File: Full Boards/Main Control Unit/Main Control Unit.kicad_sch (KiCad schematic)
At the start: 405 parts, among them J1 Optional Bond, J2 Future Use, J3 Conn_01x02_Pin, Q1 DMN6075S, Q10 DMN6075S, Q11 BSS314PE, Q12 DMN6075S, Q13 BSS314PE, Q14 DMN6075S, Q15 DMN6075S, Q2 BSS314PE, Q3 DMN6075S, Q4 BSS314PE, Q5 DMN6075S, Q6 DMN6075S, Q7 DMN6075S, Q8 DMN6075S, Q9 BSS314PE, SW1 Boot, SW2 Reset, T1 760390014, T2 760390014

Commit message: Finishing touches on the PCB layout.
Signed-off-by: digimer <digital.mermaid@gmail.com>
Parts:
- TP13: value Throttle Pots -> Throttle Pot
- TP14: value Regen Pots -> Regen Pot
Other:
- note added: "D-Sub shells are DC-floating and AC-referenced to ship ground through C83-C86"
- note removed: "Pour ground plane for GND_SH15F"
- note removed: "Pour ground plane for GND_SH15M"
- note removed: "Pour ground plane for GND_SH25F"
- note removed: "Pour ground plane for GND_SH9M"
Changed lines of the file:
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@@
 		(title "Main Control Unit")
 		(date "2026-07-29")
-		(rev "1.6.6")
+		(rev "1.6.7")
 		(company "The Digital Mermaid")
 	)
@@
 		)
 	)
-	(text "Pour ground plane for GND_SH25F"
+	(text "D-Sub shells are DC-floating and AC-referenced to ship ground through C83-C86"
 		(exclude_from_sim no)
-		(at 32.258 523.748 0)
+		(at 56.134 526.796 0)
 		(effects
 			(font
@@
 		)
 	)
-	(text "Pour ground plane for GND_SH15F"
-		(exclude_from_sim no)
-		(at 243.332 523.748 0)
-		(effects
-			(font
-				(size 1.27 1.27)
-			)
-		)
-	)
 	(text "Keep M10KW_ALARM_ISOLATED's \nDMN6075S close to nettie."
 		(exclude_from_sim no)
@@
 		)
 	)
-	(text "Pour ground plane for GND_SH9M"
-		(exclude_from_sim no)
-		(at 328.168 523.494 0)
-		(effects
-			(font
-				(size 1.27 1.27)
-			)
-		)
-	)
 	(text "E-Stop Terminal Blocks"
 		(exclude_from_sim no)
@@
 		)
 	)
-	(text "Pour ground plane for GND_SH15M"
-		(exclude_from_sim no)
-		(at 140.208 523.494 0)
-		(effects
-			(font
-				(size 1.27 1.27)
-			)
-		)
-	)
 	(text "SWD Header"
 		(exclude_from_sim no)
@@
 			)
 		)
-		(property "Value" "Throttle Pots"
+		(property "Value" "Throttle Pot"
 			(at 370.84 492.506 90)
 			(show_name no)
@@
 			)
 		)
-		(property "Value" "Regen Pots"
+		(property "Value" "Regen Pot"
 			(at 387.35 492.506 90)
 			(show_name no)

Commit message: Reworked the PCB to remove traces that blocked the GND fill on GL2.Cu.
Signed-off-by: digimer <digital.mermaid@gmail.com>
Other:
- note added: "-=] DA1 - Bottom 16. 17. 18. 19. 20. 21. 22. 23. 24. 25. 26. 27. 28. 29. 30."
- note added: "-=] DA1 - Top 1. 5KW Low Switch Out 2. 5KW Canbus Low 3. 5KW Canbus High 4. 5KW 5. 6. 7. 8. 9. 10. 11. 12. 13. 14. 15."
- note added: "-=] DA2 - Bottom 16. 17. 18. 19. 20. 21. 22. 23. 24. 25. 26. 27. 28. 29. 30."
- note added: "-=] DA2 - Top 1. 5KW Low Switch Out 2. 5KW Canbus Low 3. 5KW Canbus High 4. 5KW 5. 6. 7. 8. 9. 10. 11. 12. 13. 14. 15."
- note added: "-=] DE1 1. nc 2. RS-232 Rx 3. RS-232 Tx 4. nc 5. Ground 6. nc 7. nc 8. nc 9. nc"
- note added: "-=] DE3 1. Pump On In 2. Pump Off In 3. LED A - Pump On 4. LED A - Pump Auto 5. LED A - Pump Off 6. Ground 7. LED K - Pump On 8. LED K - Pump Auto 9. LED K - Pump Off"
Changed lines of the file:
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@@
 		(title "Main Control Unit")
 		(date "2026-07-29")
-		(rev "1.6.7")
+		(rev "1.6.8")
 		(company "The Digital Mermaid")
 	)
@@
 		)
 	)
+	(text "-=] DA2 - Bottom\n16. \n17. \n18. \n19. \n20. \n21. \n22. \n23. \n24. \n25. \n26. \n27. \n28. \n29. \n30. "
+		(exclude_from_sim no)
+		(at 231.902 569.468 0)
+		(effects
+			(font
+				(size 1.27 1.27)
+			)
+			(justify left top)
+		)
+	)
 	(text "5KW Speed High LED C"
 		(exclude_from_sim no)
@@
 		)
 	)
+	(text "-=] DA2 - Top\n 1. 5KW Low Switch Out\n 2. 5KW Canbus Low\n 3. 5KW Canbus High\n 4. 5KW \n 5. \n 6. \n 7. \n 8. \n 9. \n10. \n11. \n12. \n13. \n14. \n15. "
+		(exclude_from_sim no)
+		(at 231.902 534.67 0)
+		(effects
+			(font
+				(size 1.27 1.27)
+			)
+			(justify left top)
+		)
+	)
 	(text "LCD Display"
 		(exclude_from_sim no)
@@
 		)
 	)
+	(text "-=] DE3\n1. Pump On In\n2. Pump Off In\n3. LED A - Pump On\n4. LED A - Pump Auto\n5. LED A - Pump Off\n6. Ground\n7. LED K - Pump On\n8. LED K - Pump Auto\n9. LED K - Pump Off\n"
+		(exclude_from_sim no)
+		(at 314.706 534.67 0)
+		(effects
+			(font
+				(size 1.27 1.27)
+			)
+			(justify left top)
+		)
+	)
 	(text "10KW Speed Low LED C"
 		(exclude_from_sim no)
@@
 		)
 	)
+	(text "-=] DE1\n1. nc\n2. RS-232 Rx\n3. RS-232 Tx\n4. nc\n5. Ground\n6. nc\n7. nc\n8. nc\n9. nc\n"
+		(exclude_from_sim no)
+		(at 345.694 534.67 0)
+		(effects
+			(font
+				(size 1.27 1.27)
+			)
+			(justify left top)
+		)
+	)
 	(text "To BII1, Pin 12"
 		(exclude_from_sim no)
@@
 		)
 	)
+	(text "-=] DA1 - Top\n 1. 5KW Low Switch Out\n 2. 5KW Canbus Low\n 3. 5KW Canbus High\n 4. 5KW \n 5. \n 6. \n 7. \n 8. \n 9. \n10. \n11. \n12. \n13. \n14. \n15. "
+		(exclude_from_sim no)
+		(at 127.508 534.67 0)
+		(effects
+			(font
+				(size 1.27 1.27)
+			)
+			(justify left top)
+		)
+	)
 	(text "5KW Speed Mid LED A"
 		(exclude_from_sim no)
@@
 		)
 	)
+	(text "-=] DA1 - Bottom\n16. \n17. \n18. \n19. \n20. \n21. \n22. \n23. \n24. \n25. \n26. \n27. \n28. \n29. \n30. "
+		(exclude_from_sim no)
+		(at 127.508 569.468 0)
+		(effects
+			(font
+				(size 1.27 1.27)
+			)
+			(justify left top)
+		)
+	)

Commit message: Tagging v1.6.8
Signed-off-by: digimer <digital.mermaid@gmail.com>
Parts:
- TP13, TP14: footprint Connector_PinHeader_2.54mm:PinHeader_1x05_P2.54mm_Vertical -> Connector_PinHeader_2.54mm:PinHeader_1x03_P2.54mm_Vertical; symbol Connector:Conn_01x05_Pin -> Connector:Conn_01x03_Pin
- renumbered DE3 to DE2
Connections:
- net CA8: now also DA2.15, DA2.23
- net CA9: now also DA2.30, DA2.8
- net GND: now also TP13.2 (Pin_2), TP14.2 (Pin_2); no longer TP13.3 (Pin_3), TP14.3 (Pin_3)
- net M5KW_REGEN_POT_IN: now also TP14.3 (Pin_3); no longer TP14.5 (Pin_5)
- net THROTTLE_PORT_POT_IN: now also TP13.3 (Pin_3); no longer TP13.5 (Pin_5)
- no-connect marks 45 -> 37
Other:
- note added: "Alarm LED A"
- note added: "Alarm LED C"
- note added: "Motor Comms Lost LED A"
- note added: "Motor Comms Lost LED C"
- note removed: "-=] DA1 - Bottom 16. 17. 18. 19. 20. 21. 22. 23. 24. 25. 26. 27. 28. 29. 30."
- note removed: "-=] DA1 - Top 1. 5KW Low Switch Out 2. 5KW Canbus Low 3. 5KW Canbus High 4. 5KW 5. 6. 7. 8. 9. 10. 11. 12. 13. 14. 15."
- note removed: "-=] DA2 - Bottom 16. 17. 18. 19. 20. 21. 22. 23. 24. 25. 26. 27. 28. 29. 30."
- note removed: "-=] DA2 - Top 1. 5KW Low Switch Out 2. 5KW Canbus Low 3. 5KW Canbus High 4. 5KW 5. 6. 7. 8. 9. 10. 11. 12. 13. 14. 15."
- note removed: "-=] DE1 1. nc 2. RS-232 Rx 3. RS-232 Tx 4. nc 5. Ground 6. nc 7. nc 8. nc 9. nc"
- note removed: "-=] DE3 1. Pump On In 2. Pump Off In 3. LED A - Pump On 4. LED A - Pump Auto 5. LED A - Pump Off 6. Ground 7. LED K - Pump On 8. LED K - Pump Auto 9. LED K - Pump Off"

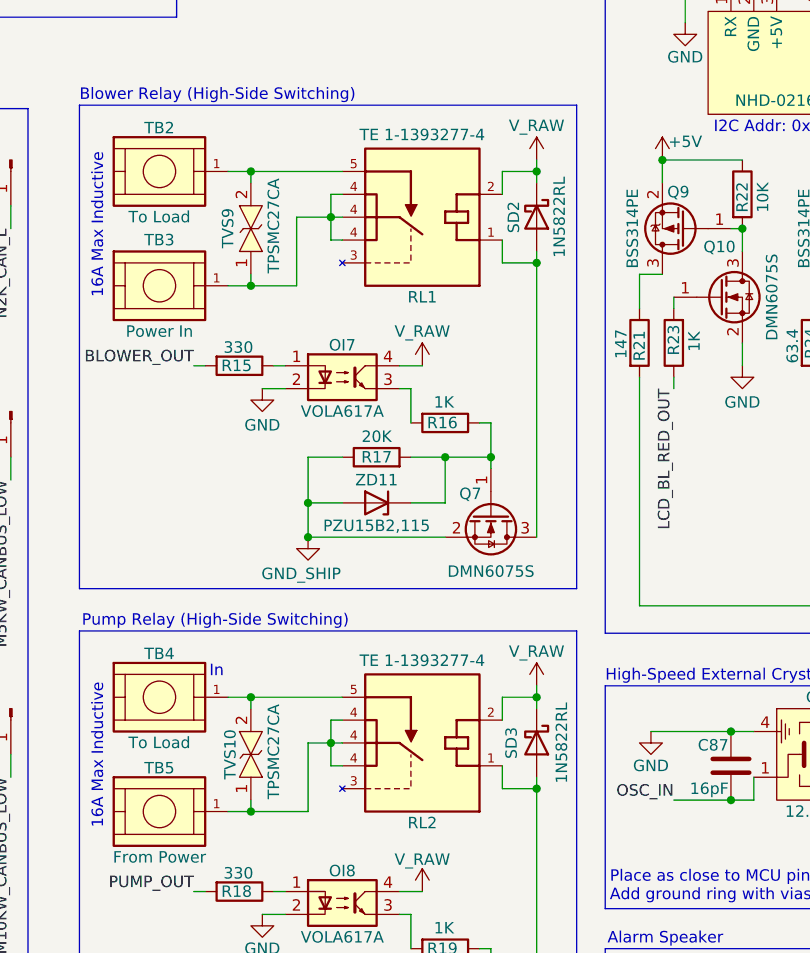
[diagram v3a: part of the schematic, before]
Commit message: Updated TE 1-1393277-4 to remove pin 3, it's not used on that specific part.
Signed-off-by: digimer <digital.mermaid@gmail.com>
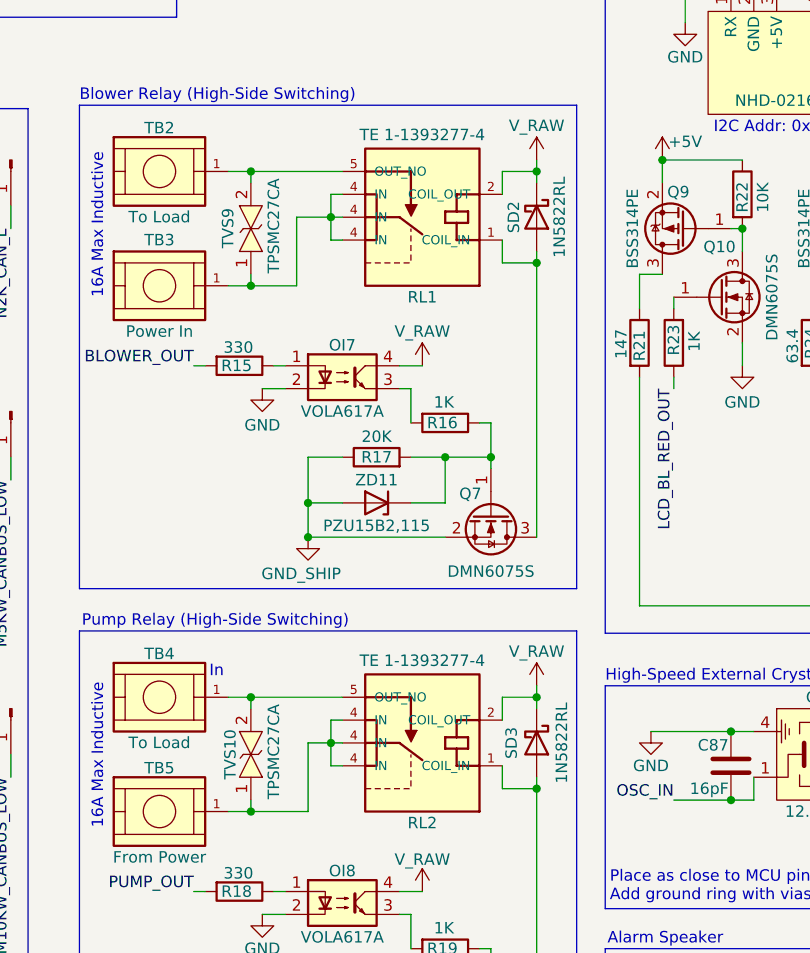
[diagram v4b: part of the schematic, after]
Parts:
- C91: Arrow Part Number Kemet C0805X101J5GACAUTO -> (none); Part DK FA18X7R1H104KNU06 -> Kemet C0805X101J5GACAUTO
- R38, R41: Part KOA Speer MF1/4CCT52R4701F -> KOA Speer MF1/4DCT52R1200F
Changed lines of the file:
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@@
 		(pin "4"
 		)
-		(pin "3"
-		)
 		(pin "5"
 		)
@@
 			)
 		)
-		(property "Part" "KOA Speer MF1/4CCT52R4701F"
+		(property "Part" "KOA Speer MF1/4DCT52R1200F"
 			(at 143.51 248.92 90)
 			(hide yes)
@@
 			)
 		)
-		(property "Part" "KOA Speer MF1/4CCT52R4701F"
+		(property "Part" "KOA Speer MF1/4DCT52R1200F"
 			(at 144.78 332.74 90)
 			(hide yes)
@@
 			)
 		)
-		(property "Part" "DK FA18X7R1H104KNU06"
-			(at 412.75 85.09 90)
-			(hide yes)
-			(show_name no)
-			(do_not_autoplace no)
-			(effects
-				(font
-					(size 1.27 1.27)
-				)
-			)
-		)
-		(property "Arrow Part Number" "Kemet C0805X101J5GACAUTO"
+		(property "Part" "Kemet C0805X101J5GACAUTO"
 			(at 412.75 85.09 0)
 			(hide yes)
@@
 		(pin "4"
 		)
-		(pin "3"
-		)
 		(pin "5"

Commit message: Fixed metadata for the 10K resistors for the LCD.
Signed-off-by: digimer <digital.mermaid@gmail.com>
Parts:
- R22, R25, R28: Part (none) -> KOA Speer MF1/4CC1002F
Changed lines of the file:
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@@
 			)
 		)
-		(property "Datasheet" ""
+		(property "Datasheet" "https://www.koaspeer.com/pdfs/MF-MFS-RK.pdf"
 			(at 349.25 88.9 0)
 			(hide yes)
@@
 			)
 		)
-		(property "Description" "Resistor"
+		(property "Description" "10 kOhms ±1% 0.25W, 1/4W Through Hole Resistor Axial Automotive AEC-Q200 Metal Film"
 			(at 349.25 88.9 0)
 			(hide yes)
@@
 			)
 		)
-		(property "Arrow Part Number" ""
-			(at 349.25 88.9 90)
-			(hide yes)
-			(show_name no)
-			(do_not_autoplace no)
-			(effects
-				(font
-					(size 1.27 1.27)
-				)
-			)
-		)
-		(property "Arrow Price/Stock" ""
-			(at 349.25 88.9 90)
-			(hide yes)
-			(show_name no)
-			(do_not_autoplace no)
-			(effects
-				(font
-					(size 1.27 1.27)
-				)
-			)
-		)
-		(property "Height" ""
-			(at 349.25 88.9 90)
-			(hide yes)
-			(show_name no)
-			(do_not_autoplace no)
-			(effects
-				(font
-					(size 1.27 1.27)
-				)
-			)
-		)
-		(property "Manufacturer_Name" ""
-			(at 349.25 88.9 90)
-			(hide yes)
-			(show_name no)
-			(do_not_autoplace no)
-			(effects
-				(font
-					(size 1.27 1.27)
-				)
-			)
-		)
-		(property "Manufacturer_Part_Number" ""
-			(at 349.25 88.9 90)
-			(hide yes)
-			(show_name no)
-			(do_not_autoplace no)
-			(effects
-				(font
-					(size 1.27 1.27)
-				)
-			)
-		)
-		(property "Mouser Part Number" ""
-			(at 349.25 88.9 90)
-			(hide yes)
-			(show_name no)
-			(do_not_autoplace no)
-			(effects
-				(font
-					(size 1.27 1.27)
-				)
-			)
-		)
-		(property "Mouser Price/Stock" ""
+		(property "Part" "KOA Speer MF1/4CC1002F"
 			(at 349.25 88.9 90)
 			(hide yes)
@@
 			)
 		)
-		(property "Datasheet" ""
+		(property "Datasheet" "https://www.koaspeer.com/pdfs/MF-MFS-RK.pdf"
 			(at 368.3 88.9 0)
 			(hide yes)
@@
 			)
 		)
-		(property "Description" "Resistor"
+		(property "Description" "10 kOhms ±1% 0.25W, 1/4W Through Hole Resistor Axial Automotive AEC-Q200 Metal Film"
 			(at 368.3 88.9 0)
 			(hide yes)
@@
 			)
 		)
-		(property "Arrow Part Number" ""
-			(at 368.3 88.9 90)
-			(hide yes)
-			(show_name no)
-			(do_not_autoplace no)
-			(effects
-				(font
-					(size 1.27 1.27)
-				)
-			)
-		)
-		(property "Arrow Price/Stock" ""
-			(at 368.3 88.9 90)
-			(hide yes)
-			(show_name no)
-			(do_not_autoplace no)
-			(effects
-				(font
-					(size 1.27 1.27)
-				)
-			)
-		)
-		(property "Height" ""
-			(at 368.3 88.9 90)
-			(hide yes)
-			(show_name no)
-			(do_not_autoplace no)
-			(effects
-				(font
-					(size 1.27 1.27)
-				)
-			)
-		)
-		(property "Manufacturer_Name" ""
-			(at 368.3 88.9 90)
-			(hide yes)
-			(show_name no)
-			(do_not_autoplace no)
-			(effects
-				(font
-					(size 1.27 1.27)
-				)
-			)
-		)
-		(property "Manufacturer_Part_Number" ""
-			(at 368.3 88.9 90)
-			(hide yes)
-			(show_name no)
-			(do_not_autoplace no)
-			(effects
-				(font
-					(size 1.27 1.27)
-				)
-			)
-		)
-		(property "Mouser Part Number" ""
-			(at 368.3 88.9 90)
-			(hide yes)
-			(show_name no)
-			(do_not_autoplace no)
-			(effects
-				(font
-					(size 1.27 1.27)
-				)
-			)
-		)
-		(property "Mouser Price/Stock" ""
+		(property "Part" "KOA Speer MF1/4CC1002F"
 			(at 368.3 88.9 90)
 			(hide yes)
@@
 			)
 		)
-		(property "Datasheet" ""
+		(property "Datasheet" "https://www.koaspeer.com/pdfs/MF-MFS-RK.pdf"
 			(at 387.35 88.9 0)
 			(hide yes)
@@
 			)
 		)
-		(property "Description" "Resistor"
+		(property "Description" "10 kOhms ±1% 0.25W, 1/4W Through Hole Resistor Axial Automotive AEC-Q200 Metal Film"
 			(at 387.35 88.9 0)
 			(hide yes)
@@
 			)
 		)
-		(property "Arrow Part Number" ""
-			(at 387.35 88.9 90)
-			(hide yes)
-			(show_name no)
-			(do_not_autoplace no)
-			(effects
-				(font
-					(size 1.27 1.27)
-				)
-			)
-		)
-		(property "Arrow Price/Stock" ""
-			(at 387.35 88.9 90)
-			(hide yes)
-			(show_name no)
-			(do_not_autoplace no)
-			(effects
-				(font
-					(size 1.27 1.27)
-				)
-			)
-		)
-		(property "Height" ""
-			(at 387.35 88.9 90)
-			(hide yes)
-			(show_name no)
-			(do_not_autoplace no)
-			(effects
-				(font
-					(size 1.27 1.27)
-				)
-			)
-		)
-		(property "Manufacturer_Name" ""
-			(at 387.35 88.9 90)
-			(hide yes)
-			(show_name no)
-			(do_not_autoplace no)
-			(effects
-				(font
-					(size 1.27 1.27)
-				)
-			)
-		)
-		(property "Manufacturer_Part_Number" ""
-			(at 387.35 88.9 90)
-			(hide yes)
-			(show_name no)
-			(do_not_autoplace no)
-			(effects
-				(font
-					(size 1.27 1.27)
-				)
-			)
-		)
-		(property "Mouser Part Number" ""
-			(at 387.35 88.9 90)
-			(hide yes)
-			(show_name no)
-			(do_not_autoplace no)
-			(effects
-				(font
-					(size 1.27 1.27)
-				)
-			)
-		)
-		(property "Mouser Price/Stock" ""
+		(property "Part" "KOA Speer MF1/4CC1002F"
 			(at 387.35 88.9 90)
 			(hide yes)
